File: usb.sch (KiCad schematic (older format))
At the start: 2 parts, among them Con5 USB_C_Wurth_632723130112, P2 USB-A-D-RA

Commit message: Added new USB connectors on schematic, figurated elements on pcb
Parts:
- removed P2: USB-A-D-RA, Connector_USB:USB-A-D-RA, symbol USB_Connectors:USB-A-D-RA
- added USB1: USB-A-Wurth-62900416021, Connector_USB:Wurth-62900416021, symbol USB_Connectors:USB-A-Wurth-62900416021
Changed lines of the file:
@@
 $EndComp
 $Comp
-L USB_Connectors:USB-A-D-RA P2
-U 1 1 6002B6FB
-P 8350 6650
-F 0 "P2" H 8878 6696 50  0000 L CNN
-F 1 "USB-A-D-RA" H 8878 6605 50  0000 L CNN
-F 2 "Connector_USB:USB-A-D-RA" H 7950 7150 50  0001 C CNN
-F 3 "C:/Wiktor/KiCad/KiCadWolowik/Schematic/Connectors/Discrete_Connectors/Components_Documentation/USB-A-D-RA.pdf" H 7950 7150 50  0001 C CNN
-	1    8350 6650
+L USB_Connectors:USB-A-Wurth-62900416021 USB1
+U 1 1 5FFFAFBC
+P 8450 6450
+F 0 "USB1" H 8678 6548 60  0000 L CNN
+F 1 "USB-A-Wurth-62900416021" H 8678 6442 60  0000 L CNN
+F 2 "Connector_USB:Wurth-62900416021" H 8250 6450 60  0001 C CNN
+F 3 "https://pl.mouser.com/datasheet/2/445/62900416021-1718169.pdf" H 8250 6450 60  0001 C CNN
+F 4 "Wurth" H 8450 6450 50  0001 C CNN "Manufacturer"
+F 5 "62900416021" H 8450 6450 50  0001 C CNN "Manufacturer Part Number"
+F 6 "Mouser" H 8450 6450 50  0001 C CNN "Supplier"
+F 7 "710-62900416021" H 8450 6400 50  0001 C CNN "Supplier Part Number"
+F 8 "https://pl.mouser.com/ProductDetail/?qs=7gQLVZk5cPluNNYrEeR0bw==" H 8450 6400 50  0001 C CNN "URL"
+F 9 "8,8" H 8450 6450 50  0001 C CNN "Price@1pc"
+F 10 "6,16" H 8450 6450 50  0001 C CNN "Price@1000pcs"
+F 11 "MW" H 8450 6450 50  0001 C CNN "Developer"
+F 12 "USB Type A Connectors SMT" H 8450 6450 50  0001 C CNN "Package"
+F 13 "" H 8450 6450 50  0001 C CNN "LCSC Part #(optional)"
+	1    8450 6450
 	1    0    0    -1
 $EndComp

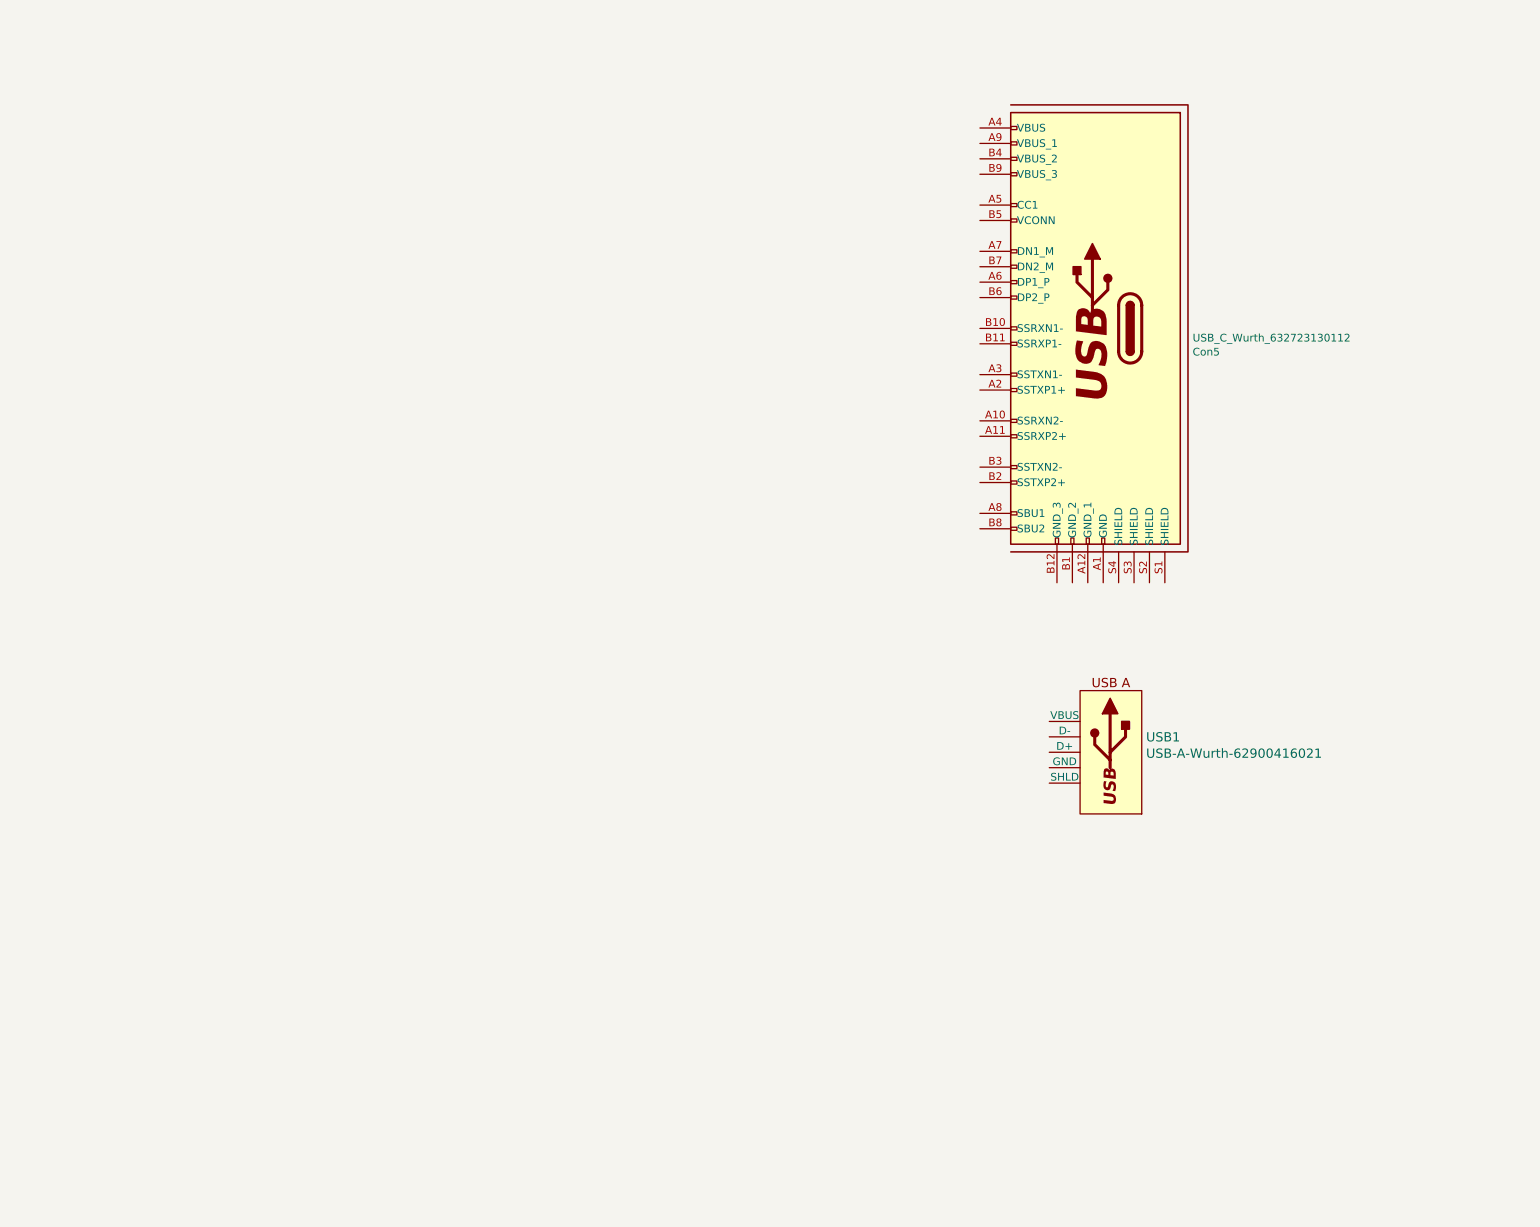
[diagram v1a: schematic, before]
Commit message: Updated schematic, added some components, figurated components on pcb
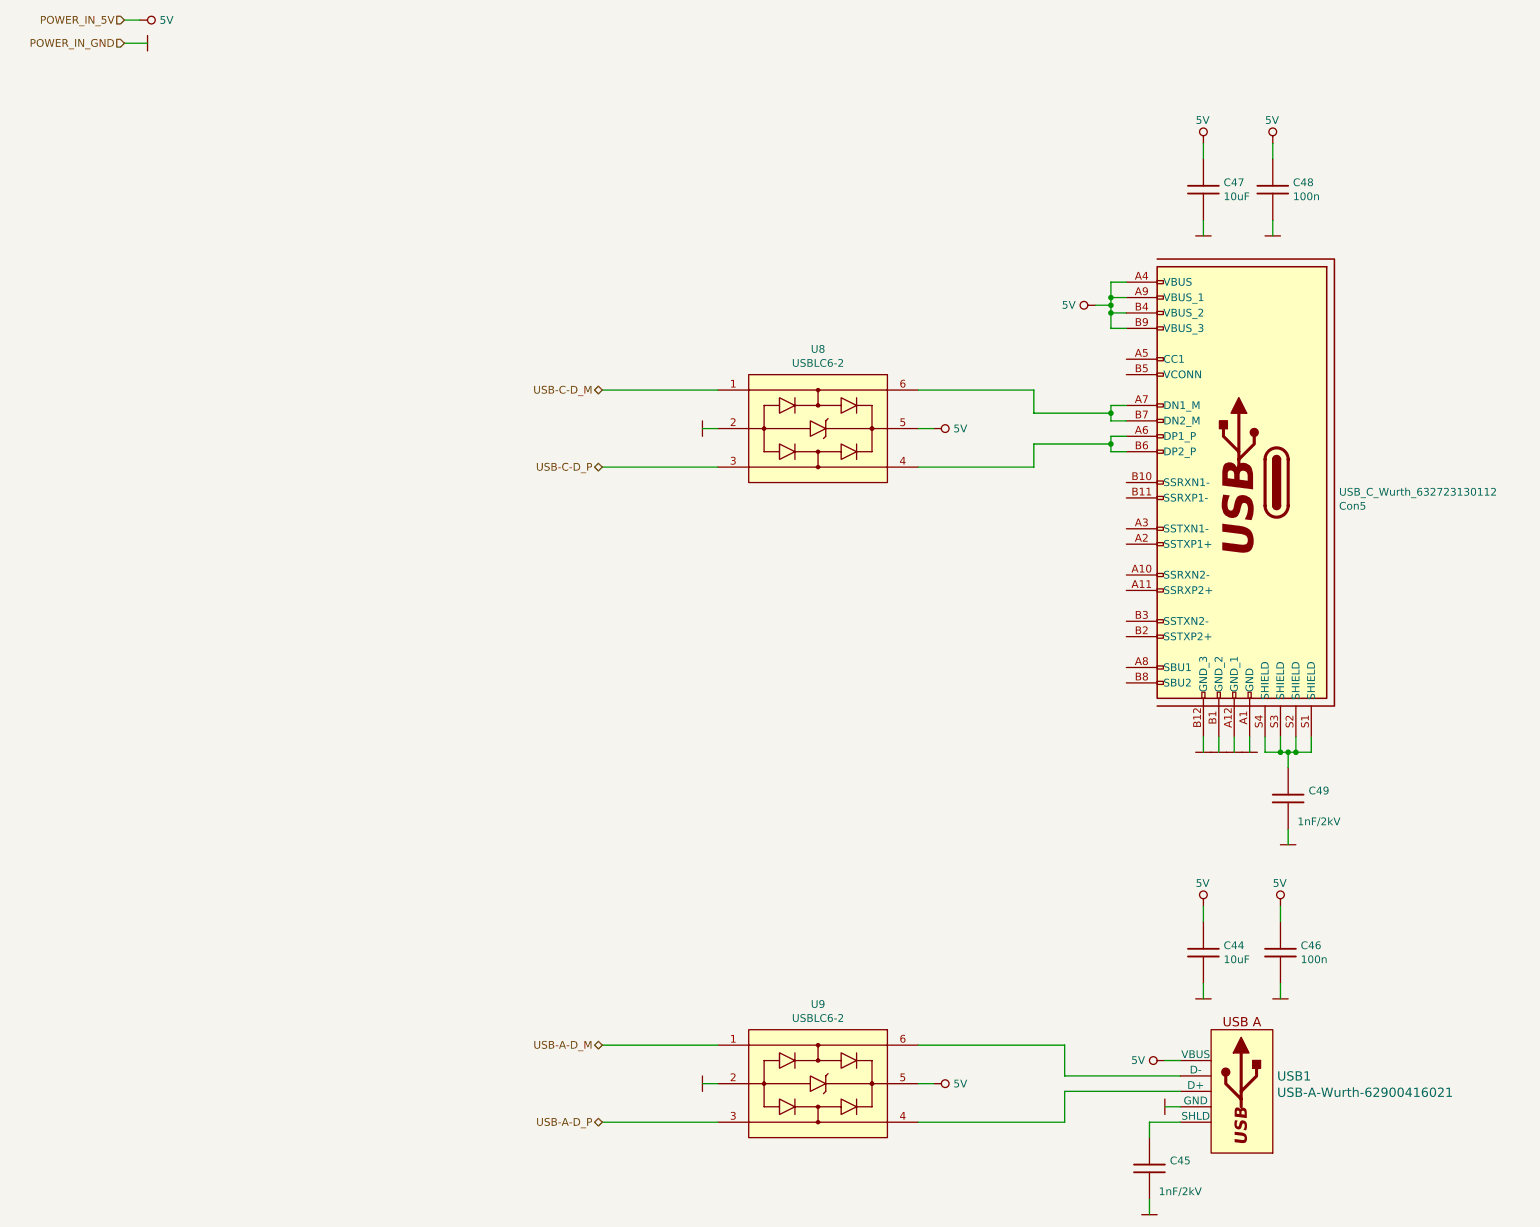
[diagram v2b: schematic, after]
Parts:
- added C44, C47: 10uF, Capacitors_Smd_0603:10uF_10V_0603, symbol Capacitors_Smd0603:10uF
- added C45, C49: 1nF/2kV, Capacitors_Smd_1206:1nF_2kV_1206, symbol Capacitors_Smd1206:1nF_2kV_1206
- added C46, C48: 100n, Capacitors_Smd_0603:100nF_0603, symbol Capacitors_Smd0603:100n
- added U8, U9: USBLC6-2, ESD_Protectors:USBLC6-2_SOT23-6L, symbol esd_protectors:USBLC6-2
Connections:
- net 5V: now reaches USB1.1 (VBUS)
- net 5V: now also Con5.A4 (VBUS), Con5.A9 (VBUS_1), Con5.B4 (VBUS_2), Con5.B9 (VBUS_3), C44.1, C46.1, C47.1, C48.1, U8.5, U9.5
- net at USB1.2 (D-): now also U9.6
- net at USB1.3 (D+): now also U9.4
- net GND: now reaches USB1.4 (GND)
- net GND: now also Con5.A1 (GND), Con5.A12 (GND_1), Con5.B1 (GND_2), Con5.B12 (GND_3), C44.2, C45.1, C46.2, C47.2, C48.2, C49.1, U8.2, U9.2
- net at USB1.SH (SHLD): now also C45.2
- net at Con5.A6 (DP1_P): now also Con5.B6 (DP2_P), U8.4
- net at Con5.A7 (DN1_M): now also Con5.B7 (DN2_M), U8.6
- net at Con5.S1 (SHIELD): now also Con5.S2 (SHIELD), Con5.S3 (SHIELD), Con5.S4 (SHIELD), C49.2
- new net USB-A-D_M: U9.1
- new net USB-A-D_P: U9.3
- new net USB-C-D_M: U8.1
- new net USB-C-D_P: U8.3
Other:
- moved on the sheet: Con5, USB1

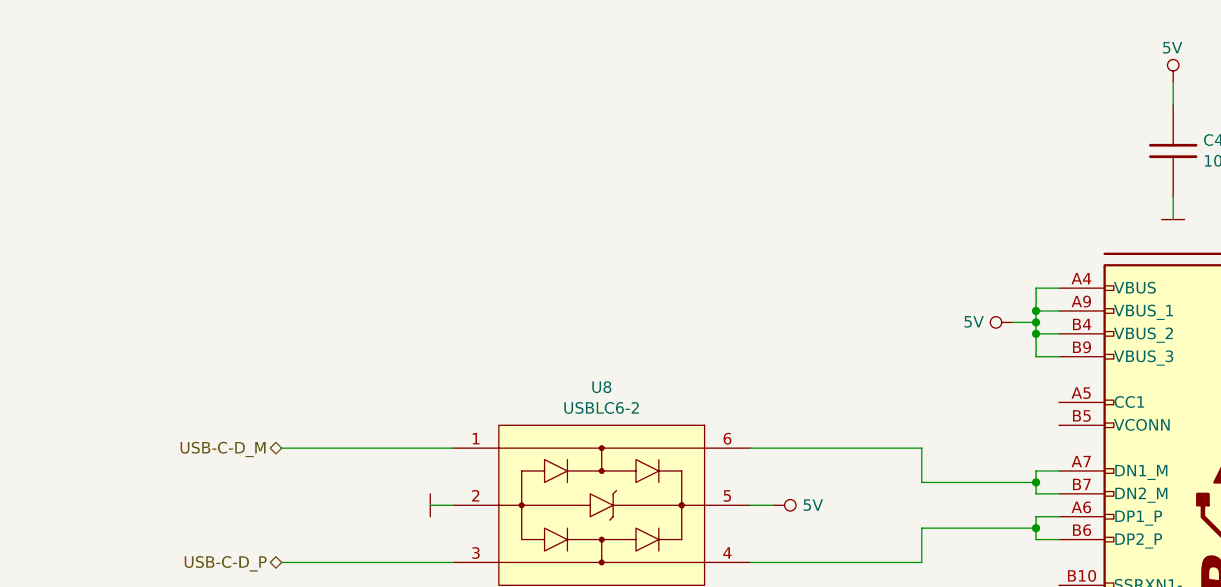
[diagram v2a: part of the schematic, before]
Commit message: Schematic work contiune, added pinout spreadsheet
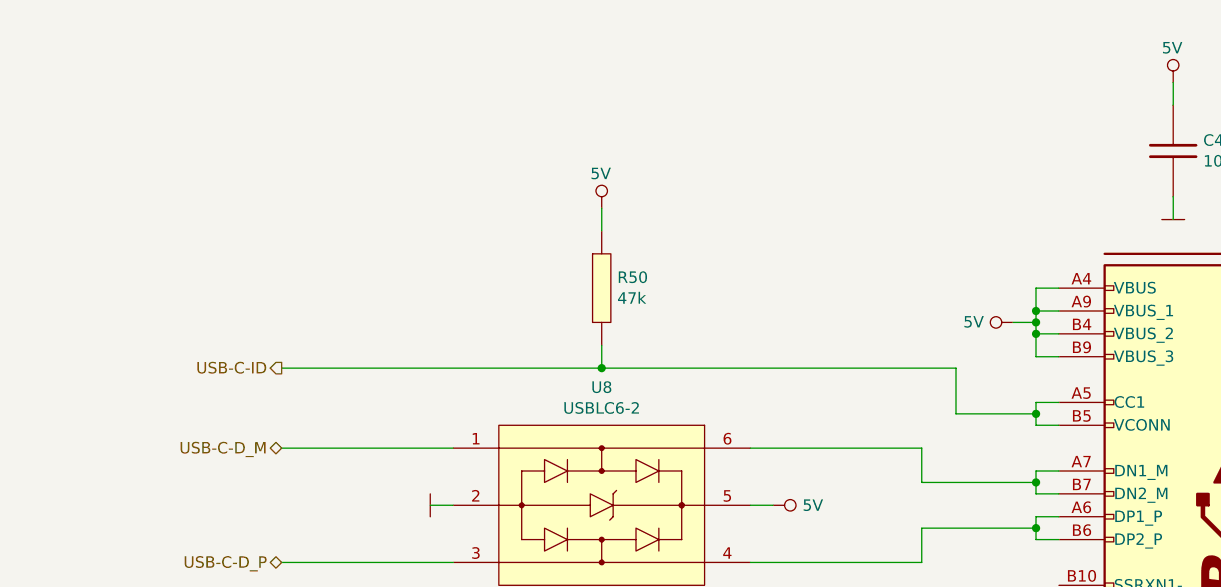
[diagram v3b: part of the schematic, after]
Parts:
- added R50: 47k, Resistor_Smd_0603:47k_0603, symbol Resistors_Smd0603:47k
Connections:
- net 5V: now also R50.1
- net USB-C-ID: now reaches Con5.A5 (CC1)
- net USB-C-ID: now also Con5.B5 (VCONN), R50.2
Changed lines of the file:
@@
 Wire Wire Line
 	8700 9450 8700 9350
+Wire Wire Line
+	8550 3900 8450 3900
+Wire Wire Line
+	8450 3900 8450 3950
+Wire Wire Line
+	8450 4000 8550 4000
+Wire Wire Line
+	8450 3950 8100 3950
+Wire Wire Line
+	8100 3950 8100 3750
+Wire Wire Line
+	8100 3750 6550 3750
+Connection ~ 8450 3950
+Wire Wire Line
+	8450 3950 8450 4000
+Text HLabel 5150 3750 0    50   Output ~ 0
+USB-C-ID
+$Comp
+L Resistors_Smd0603:47k R50
+U 1 1 60080CE5
+P 6550 3400
+F 0 "R50" H 6618 3446 50  0000 L CNN
+F 1 "47k" H 6618 3355 50  0000 L CNN
+F 2 "Resistor_Smd_0603:47k_0603" H 6550 3400 60  0001 C CNN
+F 3 "https://www.tme.eu/Document/b315665a56acbc42df513c99b390ad98/ROYALOHM-THICKFILM.pdf" H 6550 3400 60  0001 C CNN
+F 4 "Royal Ohm" H 6550 3400 50  0001 C CNN "Manufacturer"
+F 5 "0603SAF4702T5E" H 6550 3400 50  0001 C CNN "Manufacturer Part Number"
+F 6 "Tme" H 6550 3400 50  0001 C CNN "Supplier"
+F 7 "SMD0603-47K-1%" H 6550 3400 50  0001 C CNN "Supplier Part Number"
+F 8 "https://www.tme.eu/pl/details/smd0603-47k-1%25/rezystory-smd-0603/royal-ohm/0603saf4702t5e/" H 6550 3400 50  0001 C CNN "URL"
+F 9 "0,03012" H 6550 3400 50  0001 C CNN "Price@1pc"
+F 10 "0,00813" H 6550 3400 50  0001 C CNN "Price@1000pcs"
+F 11 "MW" H 6550 3400 50  0001 C CNN "Developer"
+F 12 "0603" H 6550 3400 50  0001 C CNN "Package"
+F 13 "C105579" H 6550 3400 50  0001 C CNN "LCSC Part #(optional)"
+	1    6550 3400
+	1    0    0    -1
+$EndComp
+Wire Wire Line
+	6550 3650 6550 3750
+Connection ~ 6550 3750
+Wire Wire Line
+	6550 3750 5150 3750
+$Comp
+L power:5V_NO_GLOBAL #PWR171
+U 1 1 600848EC
+P 6550 3050
+F 0 "#PWR171" V 6500 3050 20  0001 C CNN
+F 1 "5V" H 6500 3200 50  0000 L CNN
+F 2 "" H 6550 3050 60  0000 C CNN
+F 3 "" H 6550 3050 60  0000 C CNN
+	1    6550 3050
+	1    0    0    -1
+$EndComp
+Wire Wire Line
+	6550 3050 6550 3150
 $EndSCHEMATC

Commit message: Tracking in progress
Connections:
- net USB-C-ID: now also Con5.B3 (SSTXN2-)
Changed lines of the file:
@@
 Wire Wire Line
 	6550 3050 6550 3150
+Wire Wire Line
+	8550 5600 8100 5600
+Wire Wire Line
+	8100 5600 8100 3950
+Connection ~ 8100 3950
 $EndSCHEMATC

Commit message: Tracking in progress
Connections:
- net USB-A-D_M renamed USB-A-D_N
- net USB-C-D_M renamed USB-C-D_N
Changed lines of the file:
@@
 	2050 1850 2200 1850
 Text HLabel 5150 4100 0    50   BiDi ~ 0
-USB-C-D_M
+USB-C-D_N
 Text HLabel 5150 4600 0    50   BiDi ~ 0
 USB-C-D_P
@@
 	8150 8350 7200 8350
 Text HLabel 5150 8350 0    50   BiDi ~ 0
-USB-A-D_M
+USB-A-D_N
 Wire Wire Line
 	5900 8350 5150 8350

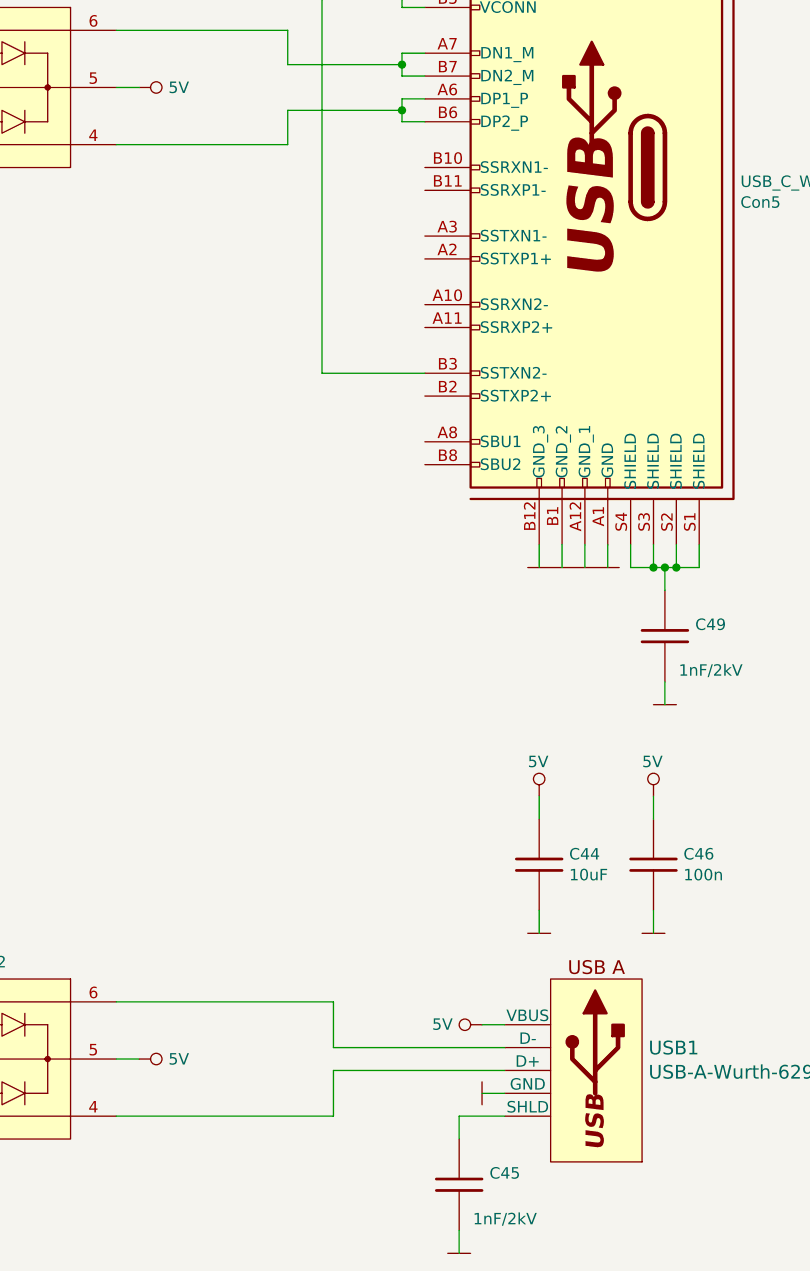
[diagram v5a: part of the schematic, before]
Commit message: Tracking finished, started tunning
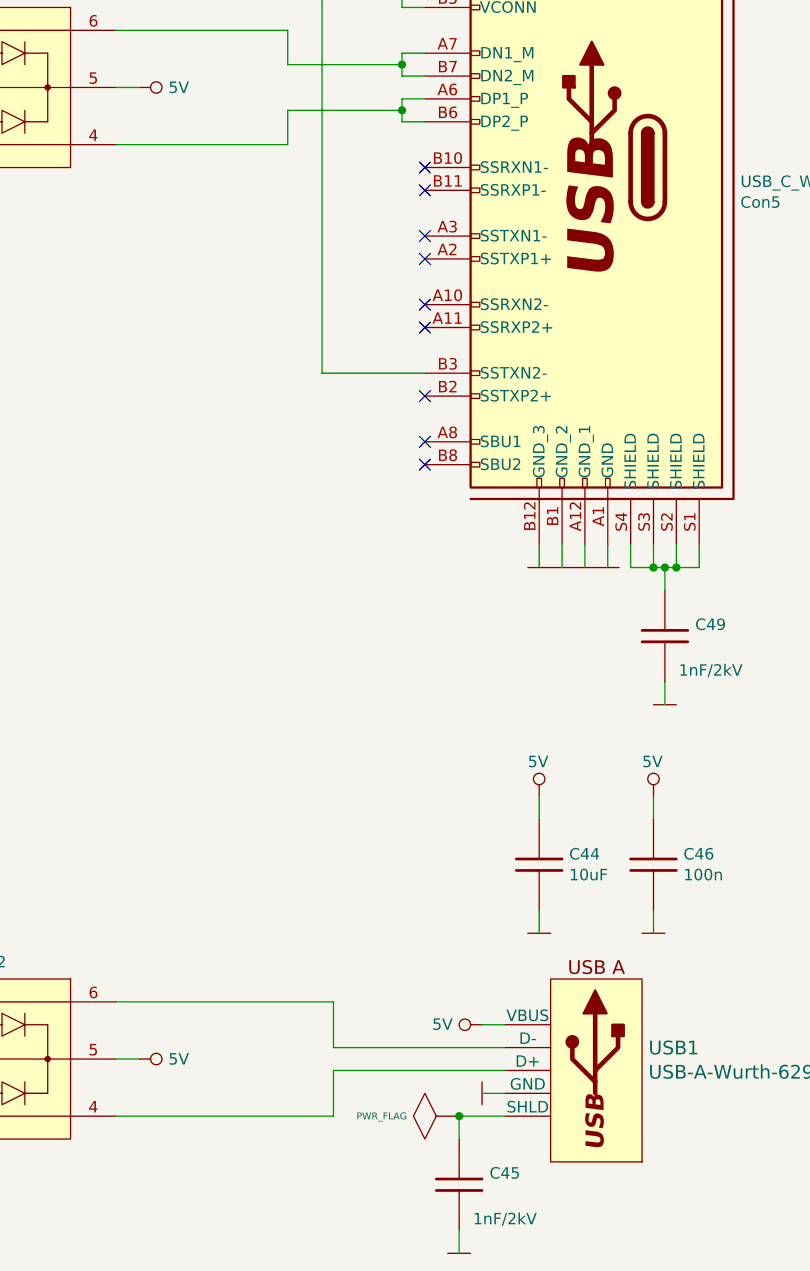
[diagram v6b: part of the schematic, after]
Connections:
- no-connect marks 0 -> 9
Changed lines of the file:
@@
 $Descr A3 16535 11693
 encoding utf-8
-Sheet 11 11
+Sheet 10 11
 Title "USB Section"
 Date "2021-01-13"
@@
 	8100 5600 8100 3950
 Connection ~ 8100 3950
+$Comp
+L power:PWR_FLAG #FLG0104
+U 1 1 600808EF
+P 8700 8850
+F 0 "#FLG0104" H 8700 9120 30  0001 C CNN
+F 1 "PWR_FLAG" V 8700 9078 30  0000 L CNN
+F 2 "" H 8700 8850 60  0000 C CNN
+F 3 "" H 8700 8850 60  0000 C CNN
+	1    8700 8850
+	0    -1   -1   0
+$EndComp
+Connection ~ 8700 8850
+NoConn ~ 8550 6000
+NoConn ~ 8550 5900
+NoConn ~ 8550 5700
+NoConn ~ 8550 5400
+NoConn ~ 8550 5300
+NoConn ~ 8550 5100
+NoConn ~ 8550 5000
+NoConn ~ 8550 4800
+NoConn ~ 8550 4700
 $EndSCHEMATC
